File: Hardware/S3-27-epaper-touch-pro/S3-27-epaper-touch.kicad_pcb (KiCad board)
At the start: 4 copper layers, 65.4 x 71 mm, 61 parts, among them J1 AFC24-S24FIC-00, J2 USB_C_Programming, J3 Conn_01x06, J4 Conn_01x06_Female, J5 Groove sensor, J6 Conn_01x06, Q1 Si1308, Q2 BC817, Q3 BC817, U1 ESP32-S3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

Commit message: Clear DRC errors
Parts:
- JP1: value →RESE -> RESE
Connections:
- J3 pad 5: /IO_8 -> /IO4_ADC1_CH3
- U1 pad 12: /IO_8 -> unconnected-(U1-Pad12)
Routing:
- net /RTS: track 104.5 -> 85.9 mm
- net /IO4_ADC1_CH3: track 0.00 -> 15.6 mm, vias 0 -> 1
- net /IO_8: track 13.4 -> 0.00 mm
- net /IO_6: track 25.5 -> 27.1 mm
- net /IO_5: track 28.5 -> 29.4 mm
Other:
- board text added: "ADC"
- board text added: "CH3"
- board text added: "IO4"
- board text added: "RAM"
- board text added: "S3 PRO SWITCH WITH TOUCH FOR GDEY027T91 GOODISPLAY"
- board text added: "→"
- board text added: "→CLK"
- board text added: "→CS"
- board text added: "→MOSI"
- board text added: "→TP.INT"
- board text removed: "C3 WALL SWITCH WITH TOUCH FOR GDEY027T91 GOODISPLAY"
- board text removed: "MOSI"
- board text removed: "→TP INT"

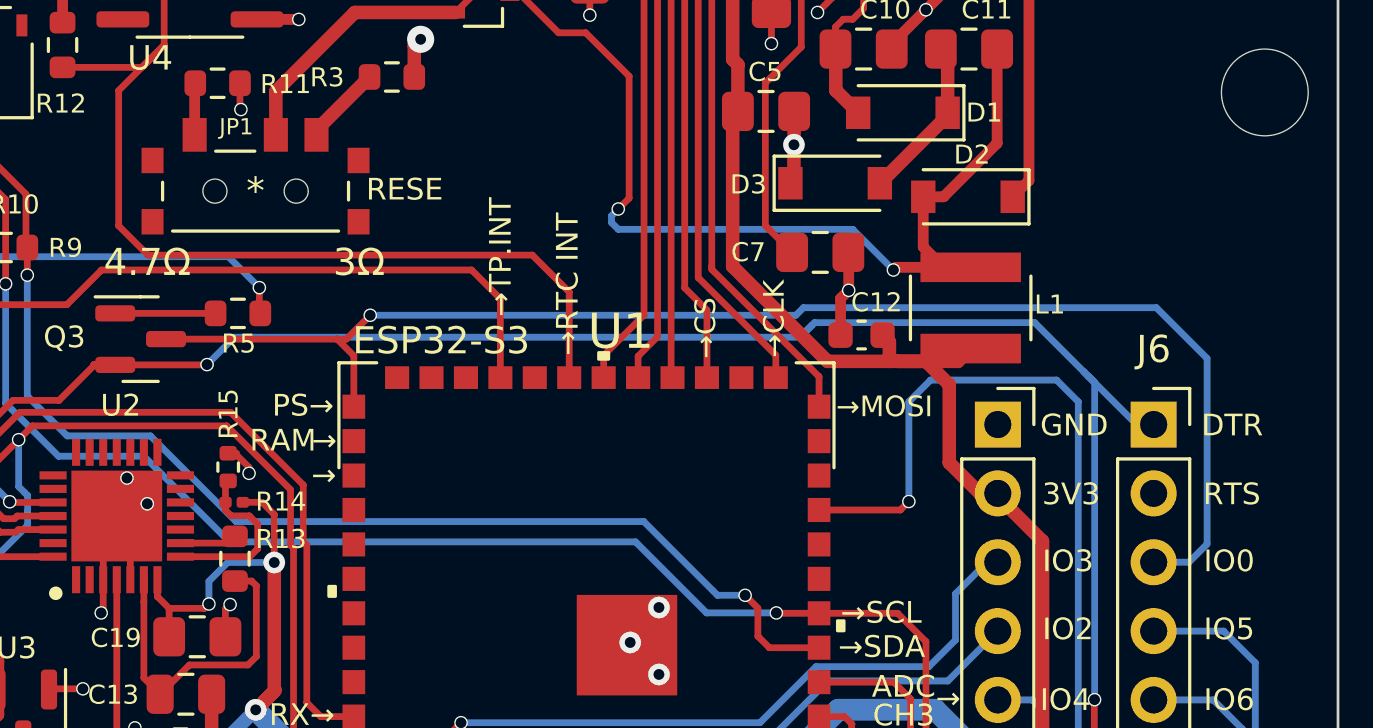
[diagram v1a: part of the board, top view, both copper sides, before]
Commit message: S3: Do not use MOSI in JTAG data pins
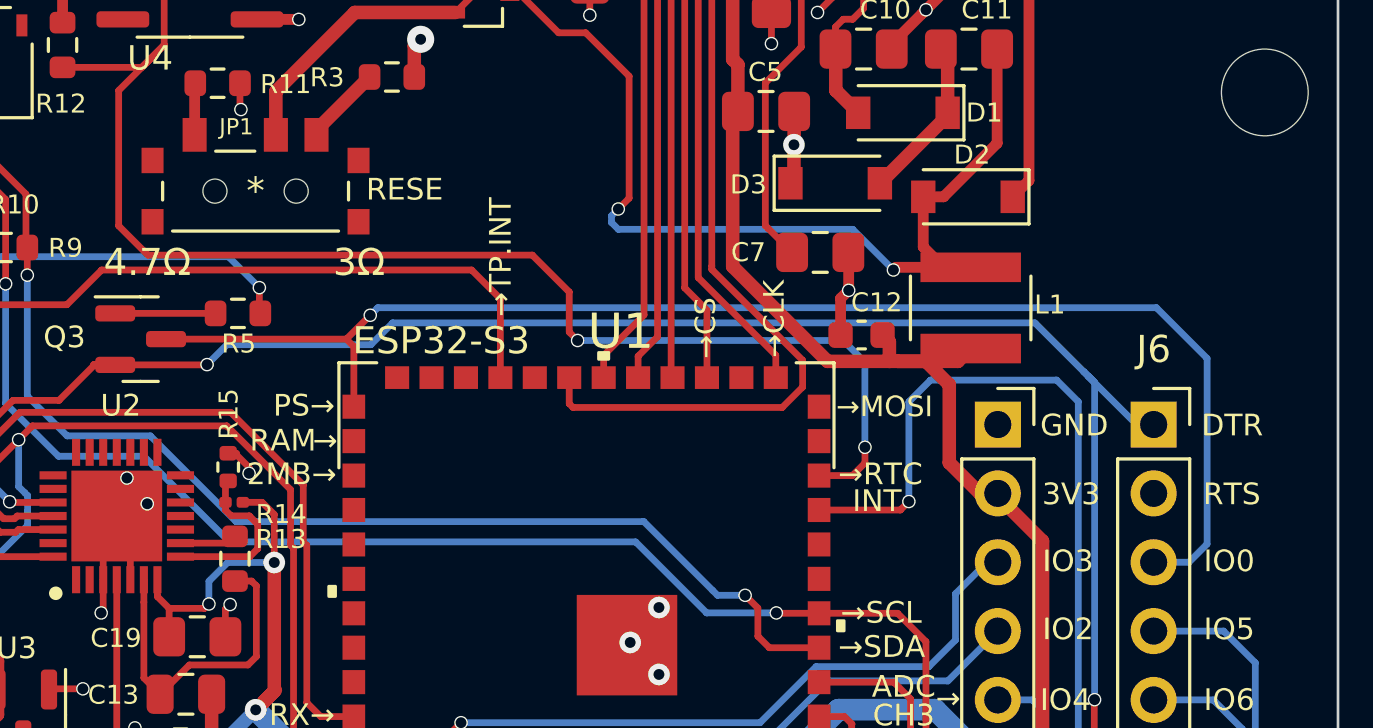
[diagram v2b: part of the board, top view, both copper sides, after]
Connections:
- U1 pad 12: unconnected-(U1-Pad12) -> /3231_INT
- U1 pad 14: /EPD_MOSI -> unconnected-(U1-Pad14)
- U1 pad 21: /3231_INT -> /EPD_MOSI
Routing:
- net /3231_INT: track 35.8 -> 51.1 mm, vias 0 -> 2
- net /EPD_MOSI: track 23.4 -> 32.4 mm
- net /DTR: track 84.9 -> 84.2 mm
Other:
- board text added: "2MB→"
- board text added: "INT"
- board text added: "→RTC"
- board text removed: "→RTC INT"

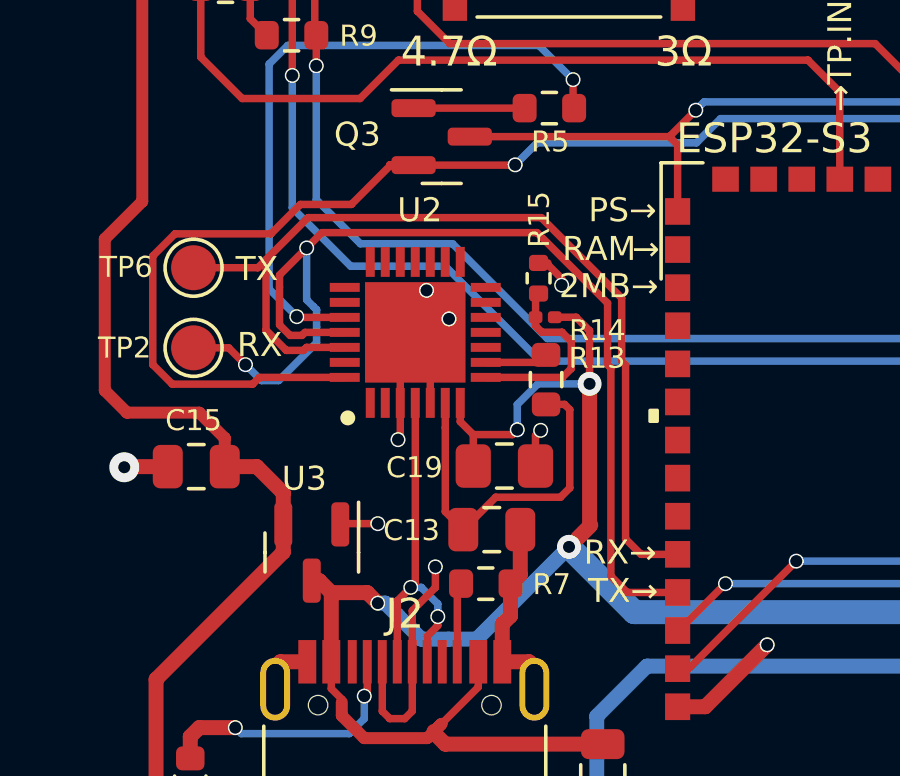
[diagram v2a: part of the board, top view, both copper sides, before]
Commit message: Update R15 thx. @Uspizig
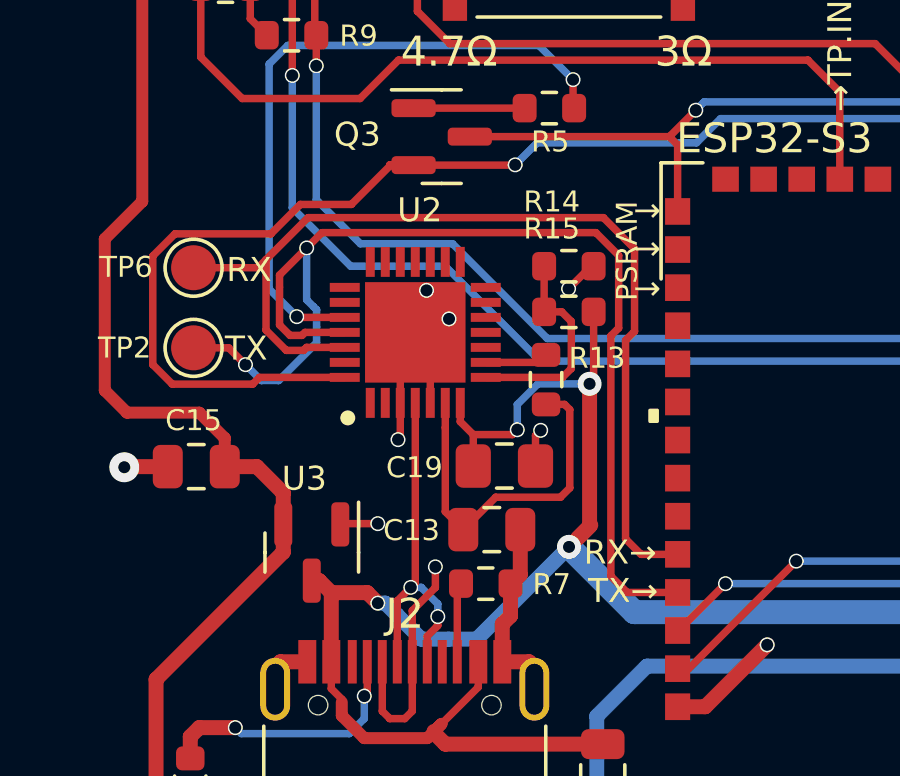
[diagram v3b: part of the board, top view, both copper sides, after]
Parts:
- R14: footprint Resistor_SMD:R_0201_0603Metric -> Resistor_SMD:R_0603_1608Metric
- R15: value 47K -> 47.5K; footprint Resistor_SMD:R_0402_1005Metric -> Resistor_SMD:R_0603_1608Metric
- moved R15 1.09 mm to (130.3, 103.5), turned to 180 degrees
- moved R14 0.81 mm to (130.3, 105.0)
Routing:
- net TX: track 31.4 -> 32.9 mm
- net RX: track 36.5 -> 37.8 mm
- net Net-(R14-Pad1): track 6.40 -> 7.10 mm
- net VBUS: track 74.0 -> 73.3 mm
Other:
- board text added: "In collaboration with DALIAN GOOD DISPLAY Team @martinfasani @GMahovlic"
- board text added: "PSRAM"
- board text added: "■ DS3231 INT → IO8 (Pulled-up w/R12) ■ I2C → SDA IO7 → SCL IO15 ■ 5V / 3V3 are power in pins. 5V input is VBUS ► U3 LDO ► 3.3V"
- board text removed: "2MB→"
- board text removed: "IN"
- board text removed: "IO1"
- board text removed: "In collaboration with DALIAN GOOD DISPLAY"
- board text removed: "PS→"
- board text removed: "RAM"
- board text removed: "■ IO2 has a 10K pullup R12 and is shared with RTC INT signal (alarm) ■ IO1 & IO3 go directly to MCU ■ 5V / 3V3 are power in pins. 5V input is VBUS ► U3 LDO ► 3.3V"

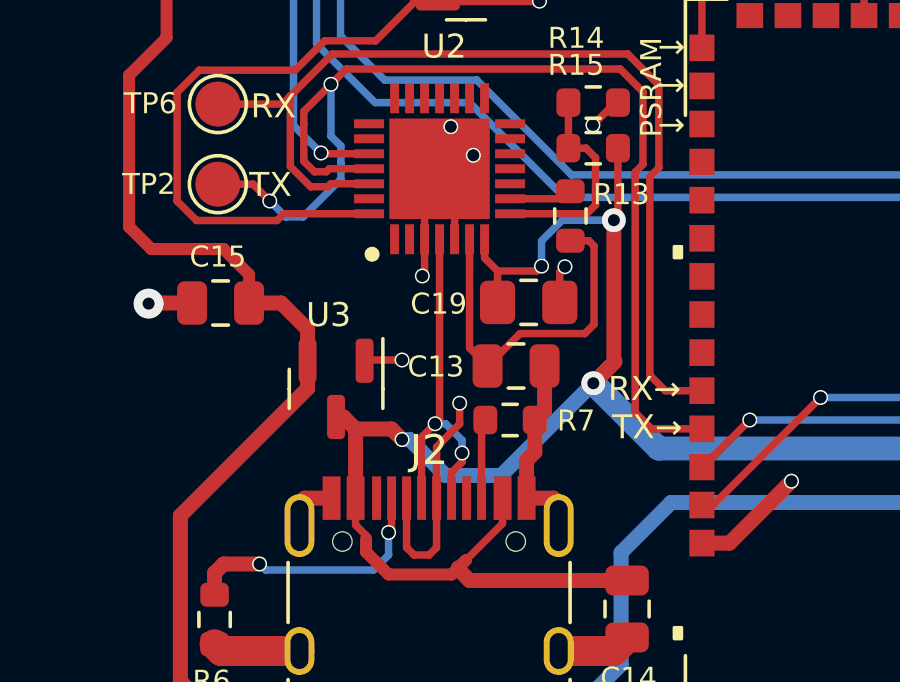
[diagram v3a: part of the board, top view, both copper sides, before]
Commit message: Error detected by @ispizig. Thanks!
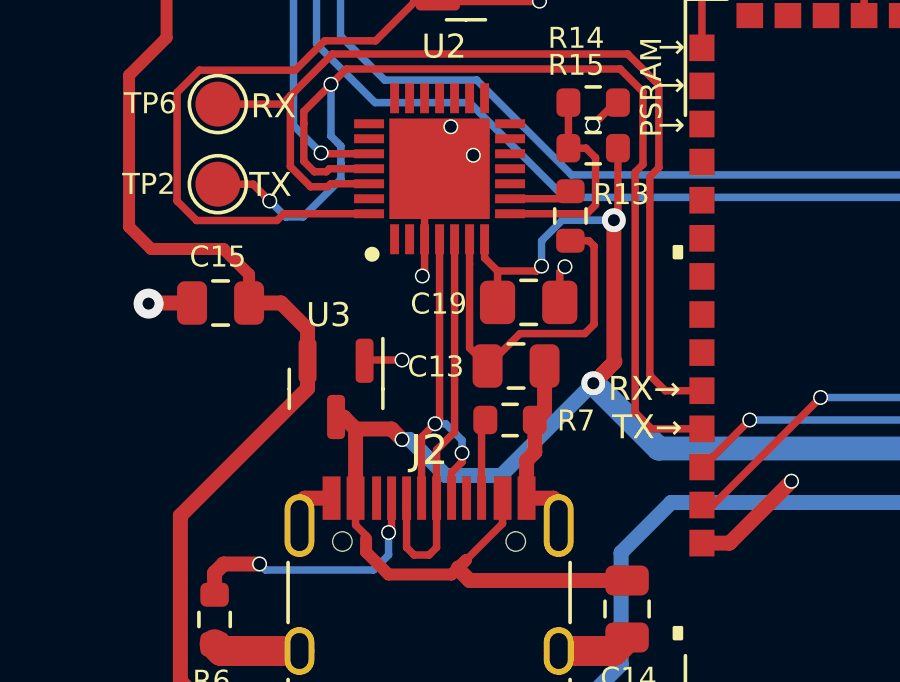
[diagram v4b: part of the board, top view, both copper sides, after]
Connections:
- J2 pad A7: GND -> Net-(J2-PadA7)
- J2 pad B7: GND -> Net-(J2-PadA7)
- U2 pad 5: GND -> Net-(J2-PadA7)
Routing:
- net Net-(J2-PadA7): track 0.00 -> 13.4 mm
- net GND: track 77.4 -> 67.6 mm, vias 29 -> 28
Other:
- board text added: "In collaboration with DALIAN GOOD DISPLAY Team PCB: @martinfasani @GMahovlic Thanks to @USpizig"
- board text removed: "In collaboration with DALIAN GOOD DISPLAY Team @martinfasani @GMahovlic"
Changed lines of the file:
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@@
   (net 90 "unconnected-(U1-Pad13)")
   (net 91 "unconnected-(U1-Pad22)")
+  (net 92 "Net-(J2-PadA7)")
   (footprint "TestPoint:TestPoint_Pad_D1.5mm" (layer "F.Cu")
     (at 156.55 82.3)
@@
     (property "Sheetfile" "S3-27-epaper-touch.kicad_sch")
     (property "Sheetname" "")
-    (attr exclude_from_pos_files exclude_from_bom)
+    (attr exclude_from_pos_files)
     (fp_text reference "TP1" (at 2.49 -1.3) (layer "F.SilkS")
       (effects (font (size 0.8 0.8) (thickness 0.13)))
@@
     (property "Sheetfile" "S3-27-epaper-touch.kicad_sch")
     (property "Sheetname" "")
-    (attr exclude_from_pos_files exclude_from_bom)
+    (attr exclude_from_pos_files)
     (fp_text reference "TP3" (at 0 -1.648) (layer "F.SilkS") hide
       (effects (font (size 0.8 0.8) (thickness 0.13)))
@@
       (net 11 "Net-(J2-PadA6)") (pinfunction "D+") (pintype "bidirectional"))
     (pad "A7" smd rect (at 0.25 -4.045) (size 0.3 1.45) (layers "F.Cu" "F.Paste" "F.Mask")
-      (net 1 "GND") (pinfunction "D-") (pintype "bidirectional"))
+      (net 92 "Net-(J2-PadA7)") (pinfunction "D-") (pintype "bidirectional"))
     (pad "A8" smd rect (at 1.25 -4.045) (size 0.3 1.45) (layers "F.Cu" "F.Paste" "F.Mask")
       (net 18 "unconnected-(J2-PadA8)") (pinfunction "SBU1") (pintype "bidirectional+no_connect"))
@@
       (net 11 "Net-(J2-PadA6)") (pinfunction "D+") (pintype "bidirectional"))
     (pad "B7" smd rect (at -0.75 -4.045) (size 0.3 1.45) (layers "F.Cu" "F.Paste" "F.Mask")
-      (net 1 "GND") (pinfunction "D-") (pintype "bidirectional"))
+      (net 92 "Net-(J2-PadA7)") (pinfunction "D-") (pintype "bidirectional"))
     (pad "B8" smd rect (at -1.75 -4.045) (size 0.3 1.45) (layers "F.Cu" "F.Paste" "F.Mask")
       (net 38 "unconnected-(J2-PadB8)") (pinfunction "SBU2") (pintype "bidirectional+no_connect"))
@@
     (property "Sheetfile" "S3-27-epaper-touch.kicad_sch")
     (property "Sheetname" "")
-    (attr exclude_from_pos_files exclude_from_bom)
+    (attr exclude_from_pos_files)
     (fp_text reference "TP4" (at 2.49 -1.1) (layer "F.SilkS")
       (effects (font (size 0.8 0.8) (thickness 0.13)))
@@
     (property "Sheetfile" "S3-27-epaper-touch.kicad_sch")
     (property "Sheetname" "")
-    (attr exclude_from_pos_files exclude_from_bom)
+    (attr exclude_from_pos_files)
     (fp_text reference "TP6" (at -2.25 -0.02) (layer "F.SilkS")
       (effects (font (size 0.7 0.7) (thickness 0.13)))
@@
     (property "Sheetfile" "S3-27-epaper-touch.kicad_sch")
     (property "Sheetname" "")
-    (attr exclude_from_pos_files exclude_from_bom)
+    (attr exclude_from_pos_files)
     (fp_text reference "TP2" (at -2.3 0) (layer "F.SilkS")
       (effects (font (size 0.7 0.7) (thickness 0.13)))
@@
       (net 11 "Net-(J2-PadA6)") (pinfunction "D+") (pintype "passive"))
     (pad "5" smd rect (at -2.35 0.5 180) (size 0.3 1) (layers "F.Cu" "F.Paste" "F.Mask")
-      (net 1 "GND") (pinfunction "D-") (pintype "passive"))
+      (net 92 "Net-(J2-PadA7)") (pinfunction "D-") (pintype "passive"))
     (pad "6" smd rect (at -2.35 1 180) (size 0.3 1) (layers "F.Cu" "F.Paste" "F.Mask")
       (net 41 "Net-(C13-Pad1)") (pinfunction "VDD") (pintype "passive"))
@@
     (property "Sheetfile" "S3-27-epaper-touch.kicad_sch")
     (property "Sheetname" "")
-    (attr through_hole exclude_from_pos_files exclude_from_bom)
+    (attr through_hole exclude_from_pos_files)
     (fp_text reference "J3" (at 3.5 -0.1) (layer "F.SilkS") hide
       (effects (font (size 1 1) (thickness 0.15)))
@@
     (property "Sheetfile" "S3-27-epaper-touch.kicad_sch")
     (property "Sheetname" "")
-    (attr exclude_from_pos_files exclude_from_bom)
+    (attr exclude_from_pos_files)
     (fp_text reference "TP5" (at 2.47 -1.28) (layer "F.SilkS")
       (effects (font (size 0.8 0.8) (thickness 0.13)))
@@
     (property "Sheetfile" "S3-27-epaper-touch.kicad_sch")
     (property "Sheetname" "")
-    (attr through_hole exclude_from_pos_files exclude_from_bom)
+    (attr through_hole exclude_from_pos_files)
     (fp_text reference "J6" (at 0 -2.77) (layer "F.SilkS")
       (effects (font (size 1 1) (thickness 0.15)))
@@
     (effects (font (size 1 1) (thickness 0.15)) (justify mirror))
   )
-  (gr_text "In collaboration with DALIAN GOOD DISPLAY\n\nTeam @martinfasani @GMahovlic" (at 157.09 90.57) (layer "B.SilkS")
+  (gr_text "In collaboration with DALIAN GOOD DISPLAY\n\nTeam PCB: @martinfasani @GMahovlic\nThanks to  @USpizig" (at 157.09 90.57) (layer "B.SilkS")
     (effects (font (size 1 1) (thickness 0.16)) (justify left mirror))
   )
@@
   (segment (start 116.9 110.2) (end 115.47 110.2) (width 0.5) (layer "F.Cu") (net 1))
   (segment (start 130.95 121.8) (end 129.12 121.8) (width 1) (layer "F.Cu") (net 1))
-  (segment (start 124.8 118.6) (end 125.05 118.35) (width 0.25) (layer "F.Cu") (net 1))
   (segment (start 151.85 99.05) (end 151.85 97.7) (width 0.4) (layer "F.Cu") (net 1))
   (segment (start 128.05 116.705) (end 128.945 116.705) (width 0.5) (layer "F.Cu") (net 1))
@@
   (segment (start 131.01 103.52) (end 130.26 104.27) (width 0.25) (layer "F.Cu") (net 1))
   (segment (start 130.325 87.405) (end 131.865 87.405) (width 0.4) (layer "F.Cu") (net 1))
-  (segment (start 124.05 116.705) (end 124.05 118.35) (width 0.25) (layer "F.Cu") (net 1))
-  (segment (start 124.05 118.35) (end 124.3 118.6) (width 0.25) (layer "F.Cu") (net 1))
   (segment (start 129.12 116.88) (end 129.12 117.62) (width 0.5) (layer "F.Cu") (net 1))
   (segment (start 123.9 112.1) (end 122.675 112.1) (width 0.25) (layer "F.Cu") (net 1))
-  (segment (start 124.3 118.6) (end 124.8 118.6) (width 0.25) (layer "F.Cu") (net 1))
   (segment (start 134.8163 118.2037) (end 136.88 116.14) (width 0.5) (layer "F.Cu") (net 1))
   (segment (start 150.13 93.32) (end 150 93.45) (width 0.5) (layer "F.Cu") (net 1))
-  (segment (start 125.82 114.23) (end 125.82 113.54) (width 0.25) (layer "F.Cu") (net 1))
   (segment (start 144.099999 79.8956) (end 144.099999 78.875001) (width 0.25) (layer "F.Cu") (net 1))
   (segment (start 128.945 116.705) (end 129.12 116.88) (width 0.5) (layer "F.Cu") (net 1))
@@
   (segment (start 128.35 114.1) (end 128.65 113.8) (width 0.5) (layer "F.Cu") (net 1))
   (segment (start 153.7375 88.3125) (end 154.85 87.2) (width 0.4) (layer "F.Cu") (net 1))
-  (segment (start 125.05 118.35) (end 125.05 116.705) (width 0.25) (layer "F.Cu") (net 1))
   (segment (start 154.85 87.2) (end 155.7875 86.2625) (width 0.4) (layer "F.Cu") (net 1))
   (segment (start 148.600001 79.8956) (end 148.600001 78.825001) (width 0.25) (layer "F.Cu") (net 1))
@@
   (segment (start 131.4 121.35) (end 130.95 121.8) (width 1) (layer "F.Cu") (net 1))
   (segment (start 151.55 86.6) (end 151 87.15) (width 0.25) (layer "F.Cu") (net 1))
-  (segment (start 125.05 116.705) (end 125.05 115) (width 0.25) (layer "F.Cu") (net 1))
   (segment (start 136.125 88.375) (end 136.36 88.14) (width 0.5) (layer "F.Cu") (net 1))
   (segment (start 157.15 69.95) (end 156.1 71) (width 0.5) (layer "F.Cu") (net 1))
@@
   (segment (start 136.2375 80.3125) (end 136.2375 78.8) (width 0.5) (layer "F.Cu") (net 1))
   (segment (start 134.02 84.53) (end 134.02 85.795) (width 0.5) (layer "F.Cu") (net 1))
-  (segment (start 125.82 114.23) (end 125.05 115) (width 0.25) (layer "F.Cu") (net 1))
   (segment (start 128.05 116.705) (end 128.05 115.45) (width 0.5) (layer "F.Cu") (net 1))
   (segment (start 133.475 83.05) (end 133.475 83.985) (width 0.5) (layer "F.Cu") (net 1))
-  (segment (start 125.65 108.075) (end 125.65 106.225) (width 0.25) (layer "F.Cu") (net 1))
   (segment (start 133.475 83.05) (end 133.5 83.05) (width 0.5) (layer "F.Cu") (net 1))
   (segment (start 159.75 69.95) (end 158.4125 69.95) (width 0.5) (layer "F.Cu") (net 1))
@@
   (via (at 142.6 87.25) (size 0.5) (drill 0.4) (layers "F.Cu" "B.Cu") (net 1))
   (via (at 136.36 88.14) (size 1) (drill 0.4) (layers "F.Cu" "B.Cu") (net 1))
-  (via (at 125.82 113.54) (size 0.5) (drill 0.4) (layers "F.Cu" "B.Cu") (net 1))
   (via (at 144.09 110.39) (size 0.8) (drill 0.4) (layers "F.Cu" "B.Cu") (net 1))
   (via (at 124.575 109.3) (size 0.5) (drill 0.4) (layers "F.Cu" "B.Cu") (net 1))
@@
   (segment (start 156.58 116.53) (end 158.54 116.53) (width 0.25) (layer "B.Cu") (net 75))
   (segment (start 158.54 116.53) (end 159.25 115.82) (width 0.25) (layer "B.Cu") (net 75))
+  (segment (start 124.8 118.6) (end 125.05 118.35) (width 0.25) (layer "F.Cu") (net 92))
+  (segment (start 125.05 115.1) (end 125.05 116.705) (width 0.25) (layer "F.Cu") (net 92))
+  (segment (start 124.05 116.705) (end 124.05 118.35) (width 0.25) (layer "F.Cu") (net 92))
+  (segment (start 124.05 118.35) (end 124.3 118.6) (width 0.25) (layer "F.Cu") (net 92))
+  (segment (start 124.3 118.6) (end 124.8 118.6) (width 0.25) (layer "F.Cu") (net 92))
+  (segment (start 125.05 118.35) (end 125.05 116.705) (width 0.25) (layer "F.Cu") (net 92))
+  (segment (start 125.65 108.075) (end 125.65 114.5) (width 0.25) (layer "F.Cu") (net 92))
+  (segment (start 125.65 114.5) (end 125.05 115.1) (width 0.25) (layer "F.Cu") (net 92))
   (zone (net 1) (net_name "GND") (layer "In1.Cu") (hatch edge 0.508)
     (connect_pads (clearance 0.508))
